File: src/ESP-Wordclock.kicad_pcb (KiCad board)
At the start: 2 copper layers, 100 x 100 mm, 1 part

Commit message: Add: BasePCB and added edge cut, holes, dimentions and LEDs with their caps
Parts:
- added BT401: CR2032, Battery:BatteryHolder_Keystone_3002_1x2032, F.Cu at (665.0, 195.0)
- added C1001: 0.1µF, Capacitor_SMD:C_0805_2012Metric_Pad1.18x1.45mm_HandSolder, F.Cu at (70.7, 105.8)
- added C1002: 0.1µF, Capacitor_SMD:C_0805_2012Metric_Pad1.18x1.45mm_HandSolder, F.Cu at (87.3, 105.8)
- added C1003: 0.1µF, Capacitor_SMD:C_0805_2012Metric_Pad1.18x1.45mm_HandSolder, F.Cu at (103.9, 105.8)
- added C1004: 0.1µF, Capacitor_SMD:C_0805_2012Metric_Pad1.18x1.45mm_HandSolder, F.Cu at (120.6, 105.8)
- added C1005: 0.1µF, Capacitor_SMD:C_0805_2012Metric_Pad1.18x1.45mm_HandSolder, F.Cu at (137.3, 105.8)
- added C1006: 0.1µF, Capacitor_SMD:C_0805_2012Metric_Pad1.18x1.45mm_HandSolder, F.Cu at (153.9, 105.8)
- added C1007: 0.1µF, Capacitor_SMD:C_0805_2012Metric_Pad1.18x1.45mm_HandSolder, F.Cu at (170.6, 105.8)
- added C1008: 0.1µF, Capacitor_SMD:C_0805_2012Metric_Pad1.18x1.45mm_HandSolder, F.Cu at (187.2, 105.8)
- added C1009: 0.1µF, Capacitor_SMD:C_0805_2012Metric_Pad1.18x1.45mm_HandSolder, F.Cu at (203.9, 105.8)
- added C1010: 0.1µF, Capacitor_SMD:C_0805_2012Metric_Pad1.18x1.45mm_HandSolder, F.Cu at (220.5, 105.8)
- added C1011: 0.1µF, Capacitor_SMD:C_0805_2012Metric_Pad1.18x1.45mm_HandSolder, F.Cu at (237.2, 105.8)
- added C1101: 0.1µF, Capacitor_SMD:C_0805_2012Metric_Pad1.18x1.45mm_HandSolder, F.Cu at (234.4, 115.8)
- added C1102: 0.1µF, Capacitor_SMD:C_0805_2012Metric_Pad1.18x1.45mm_HandSolder, F.Cu at (217.7, 115.8)
- added C1103: 0.1µF, Capacitor_SMD:C_0805_2012Metric_Pad1.18x1.45mm_HandSolder, F.Cu at (201.1, 115.8)
- added C1104: 0.1µF, Capacitor_SMD:C_0805_2012Metric_Pad1.18x1.45mm_HandSolder, F.Cu at (184.4, 115.8)
- added C1105: 0.1µF, Capacitor_SMD:C_0805_2012Metric_Pad1.18x1.45mm_HandSolder, F.Cu at (167.8, 115.8)
- added C1106: 0.1µF, Capacitor_SMD:C_0805_2012Metric_Pad1.18x1.45mm_HandSolder, F.Cu at (151.1, 115.8)
- added C1107: 0.1µF, Capacitor_SMD:C_0805_2012Metric_Pad1.18x1.45mm_HandSolder, F.Cu at (134.4, 115.8)
- added C1108: 0.1µF, Capacitor_SMD:C_0805_2012Metric_Pad1.18x1.45mm_HandSolder, F.Cu at (117.8, 115.8)
- added C1109: 0.1µF, Capacitor_SMD:C_0805_2012Metric_Pad1.18x1.45mm_HandSolder, F.Cu at (101.1, 115.8)
- added C1110: 0.1µF, Capacitor_SMD:C_0805_2012Metric_Pad1.18x1.45mm_HandSolder, F.Cu at (84.4, 115.8)
- added C1111: 0.1µF, Capacitor_SMD:C_0805_2012Metric_Pad1.18x1.45mm_HandSolder, F.Cu at (67.8, 115.8)
- added C1201: 0.1µF, Capacitor_SMD:C_0805_2012Metric_Pad1.18x1.45mm_HandSolder, F.Cu at (70.7, 142.5)
- added C1202: 0.1µF, Capacitor_SMD:C_0805_2012Metric_Pad1.18x1.45mm_HandSolder, F.Cu at (87.3, 142.5)
- added C1203: 0.1µF, Capacitor_SMD:C_0805_2012Metric_Pad1.18x1.45mm_HandSolder, F.Cu at (103.9, 142.5)
- added C1204: 0.1µF, Capacitor_SMD:C_0805_2012Metric_Pad1.18x1.45mm_HandSolder, F.Cu at (120.6, 142.5)
- added C1205: 0.1µF, Capacitor_SMD:C_0805_2012Metric_Pad1.18x1.45mm_HandSolder, F.Cu at (137.3, 142.5)
- added C1206: 0.1µF, Capacitor_SMD:C_0805_2012Metric_Pad1.18x1.45mm_HandSolder, F.Cu at (153.9, 142.5)
- added C1207: 0.1µF, Capacitor_SMD:C_0805_2012Metric_Pad1.18x1.45mm_HandSolder, F.Cu at (170.6, 142.5)
- added C1208: 0.1µF, Capacitor_SMD:C_0805_2012Metric_Pad1.18x1.45mm_HandSolder, F.Cu at (187.2, 142.5)
- added C1209: 0.1µF, Capacitor_SMD:C_0805_2012Metric_Pad1.18x1.45mm_HandSolder, F.Cu at (203.9, 142.5)
- added C1210: 0.1µF, Capacitor_SMD:C_0805_2012Metric_Pad1.18x1.45mm_HandSolder, F.Cu at (220.5, 142.5)
- added C1211: 0.1µF, Capacitor_SMD:C_0805_2012Metric_Pad1.18x1.45mm_HandSolder, F.Cu at (237.2, 142.5)
- added C1301: 0.1µF, Capacitor_SMD:C_0805_2012Metric_Pad1.18x1.45mm_HandSolder, F.Cu at (234.4, 152.5)
- added C1302: 0.1µF, Capacitor_SMD:C_0805_2012Metric_Pad1.18x1.45mm_HandSolder, F.Cu at (217.7, 152.5)
- added C1303: 0.1µF, Capacitor_SMD:C_0805_2012Metric_Pad1.18x1.45mm_HandSolder, F.Cu at (201.1, 152.5)
- added C1304: 0.1µF, Capacitor_SMD:C_0805_2012Metric_Pad1.18x1.45mm_HandSolder, F.Cu at (184.4, 152.5)
- added C1305: 0.1µF, Capacitor_SMD:C_0805_2012Metric_Pad1.18x1.45mm_HandSolder, F.Cu at (167.8, 152.5)
- added C1306: 0.1µF, Capacitor_SMD:C_0805_2012Metric_Pad1.18x1.45mm_HandSolder, F.Cu at (151.1, 152.5)
- added C1307: 0.1µF, Capacitor_SMD:C_0805_2012Metric_Pad1.18x1.45mm_HandSolder, F.Cu at (134.4, 152.5)
- added C1308: 0.1µF, Capacitor_SMD:C_0805_2012Metric_Pad1.18x1.45mm_HandSolder, F.Cu at (117.8, 152.5)
- added C1309: 0.1µF, Capacitor_SMD:C_0805_2012Metric_Pad1.18x1.45mm_HandSolder, F.Cu at (101.1, 152.5)
- added C1310: 0.1µF, Capacitor_SMD:C_0805_2012Metric_Pad1.18x1.45mm_HandSolder, F.Cu at (84.4, 152.5)
- added C1311: 0.1µF, Capacitor_SMD:C_0805_2012Metric_Pad1.18x1.45mm_HandSolder, F.Cu at (67.8, 152.5)
- added C1401: 0.1µF, Capacitor_SMD:C_0805_2012Metric_Pad1.18x1.45mm_HandSolder, F.Cu at (70.7, 179.1)
- added C1402: 0.1µF, Capacitor_SMD:C_0805_2012Metric_Pad1.18x1.45mm_HandSolder, F.Cu at (87.3, 179.1)
- added C1403: 0.1µF, Capacitor_SMD:C_0805_2012Metric_Pad1.18x1.45mm_HandSolder, F.Cu at (103.9, 179.1)
- added C1404: 0.1µF, Capacitor_SMD:C_0805_2012Metric_Pad1.18x1.45mm_HandSolder, F.Cu at (120.6, 179.1)
- added C1405: 0.1µF, Capacitor_SMD:C_0805_2012Metric_Pad1.18x1.45mm_HandSolder, F.Cu at (137.3, 179.1)
- added C1406: 0.1µF, Capacitor_SMD:C_0805_2012Metric_Pad1.18x1.45mm_HandSolder, F.Cu at (153.9, 179.1)
- added C1407: 0.1µF, Capacitor_SMD:C_0805_2012Metric_Pad1.18x1.45mm_HandSolder, F.Cu at (170.6, 179.1)
- added C1408: 0.1µF, Capacitor_SMD:C_0805_2012Metric_Pad1.18x1.45mm_HandSolder, F.Cu at (187.2, 179.1)
- added C1409: 0.1µF, Capacitor_SMD:C_0805_2012Metric_Pad1.18x1.45mm_HandSolder, F.Cu at (203.9, 179.1)
- added C1410: 0.1µF, Capacitor_SMD:C_0805_2012Metric_Pad1.18x1.45mm_HandSolder, F.Cu at (220.5, 179.1)
- added C1411: 0.1µF, Capacitor_SMD:C_0805_2012Metric_Pad1.18x1.45mm_HandSolder, F.Cu at (237.2, 179.1)
- added C1501: 0.1µF, Capacitor_SMD:C_0805_2012Metric_Pad1.18x1.45mm_HandSolder, F.Cu at (234.4, 189.2)
- added C1502: 0.1µF, Capacitor_SMD:C_0805_2012Metric_Pad1.18x1.45mm_HandSolder, F.Cu at (217.7, 189.2)
- added C1503: 0.1µF, Capacitor_SMD:C_0805_2012Metric_Pad1.18x1.45mm_HandSolder, F.Cu at (201.1, 189.2)
- added C1504: 0.1µF, Capacitor_SMD:C_0805_2012Metric_Pad1.18x1.45mm_HandSolder, F.Cu at (184.4, 189.2)
- added C1505: 0.1µF, Capacitor_SMD:C_0805_2012Metric_Pad1.18x1.45mm_HandSolder, F.Cu at (167.8, 189.2)
- added C1506: 0.1µF, Capacitor_SMD:C_0805_2012Metric_Pad1.18x1.45mm_HandSolder, F.Cu at (151.1, 189.2)
- added C1507: 0.1µF, Capacitor_SMD:C_0805_2012Metric_Pad1.18x1.45mm_HandSolder, F.Cu at (134.4, 189.2)
- added C1508: 0.1µF, Capacitor_SMD:C_0805_2012Metric_Pad1.18x1.45mm_HandSolder, F.Cu at (117.8, 189.2)
- added C1509: 0.1µF, Capacitor_SMD:C_0805_2012Metric_Pad1.18x1.45mm_HandSolder, F.Cu at (101.1, 189.2)
- added C1510: 0.1µF, Capacitor_SMD:C_0805_2012Metric_Pad1.18x1.45mm_HandSolder, F.Cu at (84.4, 189.2)
- added C1511: 0.1µF, Capacitor_SMD:C_0805_2012Metric_Pad1.18x1.45mm_HandSolder, F.Cu at (67.8, 189.2)
- added C1601: 0.1µF, Capacitor_SMD:C_0805_2012Metric_Pad1.18x1.45mm_HandSolder, F.Cu at (70.7, 215.8)
- added C1602: 0.1µF, Capacitor_SMD:C_0805_2012Metric_Pad1.18x1.45mm_HandSolder, F.Cu at (87.3, 215.8)
- added C1603: 0.1µF, Capacitor_SMD:C_0805_2012Metric_Pad1.18x1.45mm_HandSolder, F.Cu at (103.9, 215.8)
- added C1604: 0.1µF, Capacitor_SMD:C_0805_2012Metric_Pad1.18x1.45mm_HandSolder, F.Cu at (120.6, 215.8)
- added C1605: 0.1µF, Capacitor_SMD:C_0805_2012Metric_Pad1.18x1.45mm_HandSolder, F.Cu at (137.3, 215.8)
- added C1606: 0.1µF, Capacitor_SMD:C_0805_2012Metric_Pad1.18x1.45mm_HandSolder, F.Cu at (153.9, 215.8)
- added C1607: 0.1µF, Capacitor_SMD:C_0805_2012Metric_Pad1.18x1.45mm_HandSolder, F.Cu at (170.6, 215.8)
- added C1608: 0.1µF, Capacitor_SMD:C_0805_2012Metric_Pad1.18x1.45mm_HandSolder, F.Cu at (187.2, 215.8)
- added C1609: 0.1µF, Capacitor_SMD:C_0805_2012Metric_Pad1.18x1.45mm_HandSolder, F.Cu at (203.9, 215.8)
- added C1610: 0.1µF, Capacitor_SMD:C_0805_2012Metric_Pad1.18x1.45mm_HandSolder, F.Cu at (220.5, 215.8)
- added C1611: 0.1µF, Capacitor_SMD:C_0805_2012Metric_Pad1.18x1.45mm_HandSolder, F.Cu at (237.2, 215.8)
- added C1701: 0.1µF, Capacitor_SMD:C_0805_2012Metric_Pad1.18x1.45mm_HandSolder, F.Cu at (234.4, 225.9)
- added C1702: 0.1µF, Capacitor_SMD:C_0805_2012Metric_Pad1.18x1.45mm_HandSolder, F.Cu at (217.7, 225.9)
- added C1703: 0.1µF, Capacitor_SMD:C_0805_2012Metric_Pad1.18x1.45mm_HandSolder, F.Cu at (201.1, 225.9)
- added C1704: 0.1µF, Capacitor_SMD:C_0805_2012Metric_Pad1.18x1.45mm_HandSolder, F.Cu at (184.4, 225.9)
- added C1705: 0.1µF, Capacitor_SMD:C_0805_2012Metric_Pad1.18x1.45mm_HandSolder, F.Cu at (167.8, 225.9)
- added C1706: 0.1µF, Capacitor_SMD:C_0805_2012Metric_Pad1.18x1.45mm_HandSolder, F.Cu at (151.1, 225.9)
- added C1707: 0.1µF, Capacitor_SMD:C_0805_2012Metric_Pad1.18x1.45mm_HandSolder, F.Cu at (134.4, 225.9)
- added C1708: 0.1µF, Capacitor_SMD:C_0805_2012Metric_Pad1.18x1.45mm_HandSolder, F.Cu at (117.8, 225.9)
- added C1709: 0.1µF, Capacitor_SMD:C_0805_2012Metric_Pad1.18x1.45mm_HandSolder, F.Cu at (101.1, 225.9)
- added C1710: 0.1µF, Capacitor_SMD:C_0805_2012Metric_Pad1.18x1.45mm_HandSolder, F.Cu at (84.4, 225.9)
- added C1711: 0.1µF, Capacitor_SMD:C_0805_2012Metric_Pad1.18x1.45mm_HandSolder, F.Cu at (67.8, 225.9)
- added C201: 0.1µF, Capacitor_SMD:C_0805_2012Metric_Pad1.18x1.45mm_HandSolder, F.Cu at (713.3, 142.5)
- added C202: 10µF, Capacitor_SMD:C_0805_2012Metric_Pad1.18x1.45mm_HandSolder, F.Cu at (713.3, 145.5)
- added C203: 1µF, Capacitor_SMD:C_0805_2012Metric_Pad1.18x1.45mm_HandSolder, F.Cu at (713.3, 148.5)
- added C204: 10µF, Capacitor_SMD:C_0805_2012Metric_Pad1.18x1.45mm_HandSolder, F.Cu at (713.3, 151.5)
- added C205: 10µF, Capacitor_SMD:C_0805_2012Metric_Pad1.18x1.45mm_HandSolder, F.Cu at (713.3, 154.6)
- added C206: 0.1µF, Capacitor_SMD:C_0805_2012Metric_Pad1.18x1.45mm_HandSolder, F.Cu at (713.3, 157.6)
- added C207: 0.1µF, Capacitor_SMD:C_0805_2012Metric_Pad1.18x1.45mm_HandSolder, F.Cu at (713.3, 160.6)
- added C208: 0.1µF, Capacitor_SMD:C_0805_2012Metric_Pad1.18x1.45mm_HandSolder, F.Cu at (713.3, 163.6)
- added C301: 10µF, Capacitor_SMD:C_0805_2012Metric_Pad1.18x1.45mm_HandSolder, F.Cu at (516.6, 36.1)
- added C302: 0.1µF, Capacitor_SMD:C_0805_2012Metric_Pad1.18x1.45mm_HandSolder, F.Cu at (516.6, 39.1)
- added C303: 0.1µF, Capacitor_SMD:C_0805_2012Metric_Pad1.18x1.45mm_HandSolder, F.Cu at (516.6, 42.1)
- added C304: 0.1µF, Capacitor_SMD:C_0805_2012Metric_Pad1.18x1.45mm_HandSolder, F.Cu at (516.6, 45.2)
- added C305: 1µF, Capacitor_SMD:C_0805_2012Metric_Pad1.18x1.45mm_HandSolder, F.Cu at (516.6, 48.2)
- added C306: 10µF, Capacitor_SMD:C_0805_2012Metric_Pad1.18x1.45mm_HandSolder, F.Cu at (516.6, 51.2)
- added C307: 0.1µF, Capacitor_SMD:C_0805_2012Metric_Pad1.18x1.45mm_HandSolder, F.Cu at (516.6, 54.2)
- added C308: 0.1µF, Capacitor_SMD:C_0805_2012Metric_Pad1.18x1.45mm_HandSolder, F.Cu at (516.6, 57.2)
- added C309: 10µF, Capacitor_SMD:C_0805_2012Metric_Pad1.18x1.45mm_HandSolder, F.Cu at (516.6, 60.2)
- added C401: 10µF, Capacitor_SMD:C_0805_2012Metric_Pad1.18x1.45mm_HandSolder, F.Cu at (668.7, 208.1)
- added C402: 0.1µF, Capacitor_SMD:C_0805_2012Metric_Pad1.18x1.45mm_HandSolder, F.Cu at (668.7, 211.1)
- added C403: 1µF, Capacitor_SMD:C_0805_2012Metric_Pad1.18x1.45mm_HandSolder, F.Cu at (668.7, 214.1)
- added C404: 0.1µF, Capacitor_SMD:C_0805_2012Metric_Pad1.18x1.45mm_HandSolder, F.Cu at (668.7, 217.2)
- added C501: 10µF, Capacitor_SMD:C_0805_2012Metric_Pad1.18x1.45mm_HandSolder, F.Cu at (706.2, 98.6)
- added C502: 0.1µF, Capacitor_SMD:C_0805_2012Metric_Pad1.18x1.45mm_HandSolder, F.Cu at (706.2, 101.6)
- added C503: 10µF, Capacitor_SMD:C_0805_2012Metric_Pad1.18x1.45mm_HandSolder, F.Cu at (706.2, 104.7)
- added C504: 0.1µF, Capacitor_SMD:C_0805_2012Metric_Pad1.18x1.45mm_HandSolder, F.Cu at (706.2, 107.7)
- added C505: 1µF, Capacitor_SMD:C_0805_2012Metric_Pad1.18x1.45mm_HandSolder, F.Cu at (706.2, 110.7)
- added C701: 0.1µF, Capacitor_SMD:C_0805_2012Metric_Pad1.18x1.45mm_HandSolder, F.Cu at (103.9, 249.1)
- added C702: 0.1µF, Capacitor_SMD:C_0805_2012Metric_Pad1.18x1.45mm_HandSolder, F.Cu at (137.3, 249.1)
- added C703: 0.1µF, Capacitor_SMD:C_0805_2012Metric_Pad1.18x1.45mm_HandSolder, F.Cu at (170.6, 249.1)
- added C704: 0.1µF, Capacitor_SMD:C_0805_2012Metric_Pad1.18x1.45mm_HandSolder, F.Cu at (203.9, 249.1)
- added C801: 0.1µF, Capacitor_SMD:C_0805_2012Metric_Pad1.18x1.45mm_HandSolder, F.Cu at (70.7, 69.1)
- added C802: 0.1µF, Capacitor_SMD:C_0805_2012Metric_Pad1.18x1.45mm_HandSolder, F.Cu at (87.3, 69.1)
- added C803: 0.1µF, Capacitor_SMD:C_0805_2012Metric_Pad1.18x1.45mm_HandSolder, F.Cu at (103.9, 69.1)
- added C804: 0.1µF, Capacitor_SMD:C_0805_2012Metric_Pad1.18x1.45mm_HandSolder, F.Cu at (120.6, 69.1)
- added C805: 0.1µF, Capacitor_SMD:C_0805_2012Metric_Pad1.18x1.45mm_HandSolder, F.Cu at (137.3, 69.1)
- added C806: 0.1µF, Capacitor_SMD:C_0805_2012Metric_Pad1.18x1.45mm_HandSolder, F.Cu at (153.9, 69.1)
- added C807: 0.1µF, Capacitor_SMD:C_0805_2012Metric_Pad1.18x1.45mm_HandSolder, F.Cu at (170.6, 69.1)
- added C808: 0.1µF, Capacitor_SMD:C_0805_2012Metric_Pad1.18x1.45mm_HandSolder, F.Cu at (187.2, 69.1)
- added C809: 0.1µF, Capacitor_SMD:C_0805_2012Metric_Pad1.18x1.45mm_HandSolder, F.Cu at (203.9, 69.1)
- added C810: 0.1µF, Capacitor_SMD:C_0805_2012Metric_Pad1.18x1.45mm_HandSolder, F.Cu at (220.5, 69.1)
- added C811: 0.1µF, Capacitor_SMD:C_0805_2012Metric_Pad1.18x1.45mm_HandSolder, F.Cu at (237.2, 69.1)
- added C901: 0.1µF, Capacitor_SMD:C_0805_2012Metric_Pad1.18x1.45mm_HandSolder, F.Cu at (234.4, 79.2)
- added C902: 0.1µF, Capacitor_SMD:C_0805_2012Metric_Pad1.18x1.45mm_HandSolder, F.Cu at (217.7, 79.2)
- added C903: 0.1µF, Capacitor_SMD:C_0805_2012Metric_Pad1.18x1.45mm_HandSolder, F.Cu at (201.1, 79.2)
- added C904: 0.1µF, Capacitor_SMD:C_0805_2012Metric_Pad1.18x1.45mm_HandSolder, F.Cu at (184.4, 79.2)
- added C905: 0.1µF, Capacitor_SMD:C_0805_2012Metric_Pad1.18x1.45mm_HandSolder, F.Cu at (167.8, 79.2)
- added C906: 0.1µF, Capacitor_SMD:C_0805_2012Metric_Pad1.18x1.45mm_HandSolder, F.Cu at (151.1, 79.2)
- added C907: 0.1µF, Capacitor_SMD:C_0805_2012Metric_Pad1.18x1.45mm_HandSolder, F.Cu at (134.4, 79.2)
- added C908: 0.1µF, Capacitor_SMD:C_0805_2012Metric_Pad1.18x1.45mm_HandSolder, F.Cu at (117.8, 79.2)
- added C909: 0.1µF, Capacitor_SMD:C_0805_2012Metric_Pad1.18x1.45mm_HandSolder, F.Cu at (101.1, 79.2)
- added C910: 0.1µF, Capacitor_SMD:C_0805_2012Metric_Pad1.18x1.45mm_HandSolder, F.Cu at (84.4, 79.2)
- added C911: 0.1µF, Capacitor_SMD:C_0805_2012Metric_Pad1.18x1.45mm_HandSolder, F.Cu at (67.8, 79.2)
- added D1001: WS2812B, LED_SMD:LED_WS2812B_PLCC4_5.0x5.0mm_P3.2mm, F.Cu at (69.2, 101.7)
- added D1002: WS2812B, LED_SMD:LED_WS2812B_PLCC4_5.0x5.0mm_P3.2mm, F.Cu at (85.9, 101.7)
- added D1003: WS2812B, LED_SMD:LED_WS2812B_PLCC4_5.0x5.0mm_P3.2mm, F.Cu at (102.5, 101.7)
- added D1004: WS2812B, LED_SMD:LED_WS2812B_PLCC4_5.0x5.0mm_P3.2mm, F.Cu at (119.2, 101.7)
- added D1005: WS2812B, LED_SMD:LED_WS2812B_PLCC4_5.0x5.0mm_P3.2mm, F.Cu at (135.8, 101.7)
- added D1006: WS2812B, LED_SMD:LED_WS2812B_PLCC4_5.0x5.0mm_P3.2mm, F.Cu at (152.5, 101.7)
- added D1007: WS2812B, LED_SMD:LED_WS2812B_PLCC4_5.0x5.0mm_P3.2mm, F.Cu at (169.2, 101.7)
- added D1008: WS2812B, LED_SMD:LED_WS2812B_PLCC4_5.0x5.0mm_P3.2mm, F.Cu at (185.8, 101.7)
- added D1009: WS2812B, LED_SMD:LED_WS2812B_PLCC4_5.0x5.0mm_P3.2mm, F.Cu at (202.5, 101.7)
- added D1010: WS2812B, LED_SMD:LED_WS2812B_PLCC4_5.0x5.0mm_P3.2mm, F.Cu at (219.1, 101.7)
- added D1011: WS2812B, LED_SMD:LED_WS2812B_PLCC4_5.0x5.0mm_P3.2mm, F.Cu at (235.8, 101.7)
- added D1101: WS2812B, LED_SMD:LED_WS2812B_PLCC4_5.0x5.0mm_P3.2mm, F.Cu at (235.8, 120.0)
- added D1102: WS2812B, LED_SMD:LED_WS2812B_PLCC4_5.0x5.0mm_P3.2mm, F.Cu at (219.1, 120.0)
- added D1103: WS2812B, LED_SMD:LED_WS2812B_PLCC4_5.0x5.0mm_P3.2mm, F.Cu at (202.5, 120.0)
- added D1104: WS2812B, LED_SMD:LED_WS2812B_PLCC4_5.0x5.0mm_P3.2mm, F.Cu at (185.8, 120.0)
- added D1105: WS2812B, LED_SMD:LED_WS2812B_PLCC4_5.0x5.0mm_P3.2mm, F.Cu at (169.2, 120.0)
- added D1106: WS2812B, LED_SMD:LED_WS2812B_PLCC4_5.0x5.0mm_P3.2mm, F.Cu at (152.5, 120.0)
- added D1107: WS2812B, LED_SMD:LED_WS2812B_PLCC4_5.0x5.0mm_P3.2mm, F.Cu at (135.8, 120.0)
- added D1108: WS2812B, LED_SMD:LED_WS2812B_PLCC4_5.0x5.0mm_P3.2mm, F.Cu at (119.2, 120.0)
- added D1109: WS2812B, LED_SMD:LED_WS2812B_PLCC4_5.0x5.0mm_P3.2mm, F.Cu at (102.5, 120.0)
- added D1110: WS2812B, LED_SMD:LED_WS2812B_PLCC4_5.0x5.0mm_P3.2mm, F.Cu at (85.9, 120.0)
- added D1111: WS2812B, LED_SMD:LED_WS2812B_PLCC4_5.0x5.0mm_P3.2mm, F.Cu at (69.2, 120.0)
- added D1201: WS2812B, LED_SMD:LED_WS2812B_PLCC4_5.0x5.0mm_P3.2mm, F.Cu at (69.2, 138.3)
- added D1202: WS2812B, LED_SMD:LED_WS2812B_PLCC4_5.0x5.0mm_P3.2mm, F.Cu at (85.9, 138.3)
- added D1203: WS2812B, LED_SMD:LED_WS2812B_PLCC4_5.0x5.0mm_P3.2mm, F.Cu at (102.5, 138.3)
- added D1204: WS2812B, LED_SMD:LED_WS2812B_PLCC4_5.0x5.0mm_P3.2mm, F.Cu at (119.2, 138.3)
- added D1205: WS2812B, LED_SMD:LED_WS2812B_PLCC4_5.0x5.0mm_P3.2mm, F.Cu at (135.8, 138.3)
- added D1206: WS2812B, LED_SMD:LED_WS2812B_PLCC4_5.0x5.0mm_P3.2mm, F.Cu at (152.5, 138.3)
- added D1207: WS2812B, LED_SMD:LED_WS2812B_PLCC4_5.0x5.0mm_P3.2mm, F.Cu at (169.2, 138.3)
- added D1208: WS2812B, LED_SMD:LED_WS2812B_PLCC4_5.0x5.0mm_P3.2mm, F.Cu at (185.8, 138.3)
- added D1209: WS2812B, LED_SMD:LED_WS2812B_PLCC4_5.0x5.0mm_P3.2mm, F.Cu at (202.5, 138.3)
- added D1210: WS2812B, LED_SMD:LED_WS2812B_PLCC4_5.0x5.0mm_P3.2mm, F.Cu at (219.1, 138.3)
- added D1211: WS2812B, LED_SMD:LED_WS2812B_PLCC4_5.0x5.0mm_P3.2mm, F.Cu at (235.8, 138.3)
- added D1301: WS2812B, LED_SMD:LED_WS2812B_PLCC4_5.0x5.0mm_P3.2mm, F.Cu at (235.8, 156.7)
- added D1302: WS2812B, LED_SMD:LED_WS2812B_PLCC4_5.0x5.0mm_P3.2mm, F.Cu at (219.1, 156.7)
- added D1303: WS2812B, LED_SMD:LED_WS2812B_PLCC4_5.0x5.0mm_P3.2mm, F.Cu at (202.5, 156.7)
- added D1304: WS2812B, LED_SMD:LED_WS2812B_PLCC4_5.0x5.0mm_P3.2mm, F.Cu at (185.8, 156.7)
- added D1305: WS2812B, LED_SMD:LED_WS2812B_PLCC4_5.0x5.0mm_P3.2mm, F.Cu at (169.2, 156.7)
- added D1306: WS2812B, LED_SMD:LED_WS2812B_PLCC4_5.0x5.0mm_P3.2mm, F.Cu at (152.5, 156.7)
- added D1307: WS2812B, LED_SMD:LED_WS2812B_PLCC4_5.0x5.0mm_P3.2mm, F.Cu at (135.8, 156.7)
- added D1308: WS2812B, LED_SMD:LED_WS2812B_PLCC4_5.0x5.0mm_P3.2mm, F.Cu at (119.2, 156.7)
- added D1309: WS2812B, LED_SMD:LED_WS2812B_PLCC4_5.0x5.0mm_P3.2mm, F.Cu at (102.5, 156.7)
- added D1310: WS2812B, LED_SMD:LED_WS2812B_PLCC4_5.0x5.0mm_P3.2mm, F.Cu at (85.9, 156.7)
- added D1311: WS2812B, LED_SMD:LED_WS2812B_PLCC4_5.0x5.0mm_P3.2mm, F.Cu at (69.2, 156.7)
- added D1401: WS2812B, LED_SMD:LED_WS2812B_PLCC4_5.0x5.0mm_P3.2mm, F.Cu at (69.2, 175.0)
- added D1402: WS2812B, LED_SMD:LED_WS2812B_PLCC4_5.0x5.0mm_P3.2mm, F.Cu at (85.9, 175.0)
- added D1403: WS2812B, LED_SMD:LED_WS2812B_PLCC4_5.0x5.0mm_P3.2mm, F.Cu at (102.5, 175.0)
- added D1404: WS2812B, LED_SMD:LED_WS2812B_PLCC4_5.0x5.0mm_P3.2mm, F.Cu at (119.2, 175.0)
- added D1405: WS2812B, LED_SMD:LED_WS2812B_PLCC4_5.0x5.0mm_P3.2mm, F.Cu at (135.8, 175.0)
- added D1406: WS2812B, LED_SMD:LED_WS2812B_PLCC4_5.0x5.0mm_P3.2mm, F.Cu at (152.5, 175.0)
- added D1407: WS2812B, LED_SMD:LED_WS2812B_PLCC4_5.0x5.0mm_P3.2mm, F.Cu at (169.2, 175.0)
- added D1408: WS2812B, LED_SMD:LED_WS2812B_PLCC4_5.0x5.0mm_P3.2mm, F.Cu at (185.8, 175.0)
- added D1409: WS2812B, LED_SMD:LED_WS2812B_PLCC4_5.0x5.0mm_P3.2mm, F.Cu at (202.5, 175.0)
- added D1410: WS2812B, LED_SMD:LED_WS2812B_PLCC4_5.0x5.0mm_P3.2mm, F.Cu at (219.1, 175.0)
- added D1411: WS2812B, LED_SMD:LED_WS2812B_PLCC4_5.0x5.0mm_P3.2mm, F.Cu at (235.8, 175.0)
- added D1501: WS2812B, LED_SMD:LED_WS2812B_PLCC4_5.0x5.0mm_P3.2mm, F.Cu at (235.8, 193.3)
- added D1502: WS2812B, LED_SMD:LED_WS2812B_PLCC4_5.0x5.0mm_P3.2mm, F.Cu at (219.1, 193.3)
- added D1503: WS2812B, LED_SMD:LED_WS2812B_PLCC4_5.0x5.0mm_P3.2mm, F.Cu at (202.5, 193.3)
- added D1504: WS2812B, LED_SMD:LED_WS2812B_PLCC4_5.0x5.0mm_P3.2mm, F.Cu at (185.8, 193.3)
- added D1505: WS2812B, LED_SMD:LED_WS2812B_PLCC4_5.0x5.0mm_P3.2mm, F.Cu at (169.2, 193.3)
- added D1506: WS2812B, LED_SMD:LED_WS2812B_PLCC4_5.0x5.0mm_P3.2mm, F.Cu at (152.5, 193.3)
- added D1507: WS2812B, LED_SMD:LED_WS2812B_PLCC4_5.0x5.0mm_P3.2mm, F.Cu at (135.8, 193.3)
- added D1508: WS2812B, LED_SMD:LED_WS2812B_PLCC4_5.0x5.0mm_P3.2mm, F.Cu at (119.2, 193.3)
- added D1509: WS2812B, LED_SMD:LED_WS2812B_PLCC4_5.0x5.0mm_P3.2mm, F.Cu at (102.5, 193.3)
- added D1510: WS2812B, LED_SMD:LED_WS2812B_PLCC4_5.0x5.0mm_P3.2mm, F.Cu at (85.9, 193.3)
- added D1511: WS2812B, LED_SMD:LED_WS2812B_PLCC4_5.0x5.0mm_P3.2mm, F.Cu at (69.2, 193.3)
- added D1601: WS2812B, LED_SMD:LED_WS2812B_PLCC4_5.0x5.0mm_P3.2mm, F.Cu at (69.2, 211.7)
- added D1602: WS2812B, LED_SMD:LED_WS2812B_PLCC4_5.0x5.0mm_P3.2mm, F.Cu at (85.9, 211.7)
- added D1603: WS2812B, LED_SMD:LED_WS2812B_PLCC4_5.0x5.0mm_P3.2mm, F.Cu at (102.5, 211.7)
- added D1604: WS2812B, LED_SMD:LED_WS2812B_PLCC4_5.0x5.0mm_P3.2mm, F.Cu at (119.2, 211.7)
- added D1605: WS2812B, LED_SMD:LED_WS2812B_PLCC4_5.0x5.0mm_P3.2mm, F.Cu at (135.8, 211.7)
- added D1606: WS2812B, LED_SMD:LED_WS2812B_PLCC4_5.0x5.0mm_P3.2mm, F.Cu at (152.5, 211.7)
- added D1607: WS2812B, LED_SMD:LED_WS2812B_PLCC4_5.0x5.0mm_P3.2mm, F.Cu at (169.2, 211.7)
- added D1608: WS2812B, LED_SMD:LED_WS2812B_PLCC4_5.0x5.0mm_P3.2mm, F.Cu at (185.8, 211.7)
- added D1609: WS2812B, LED_SMD:LED_WS2812B_PLCC4_5.0x5.0mm_P3.2mm, F.Cu at (202.5, 211.7)
- added D1610: WS2812B, LED_SMD:LED_WS2812B_PLCC4_5.0x5.0mm_P3.2mm, F.Cu at (219.1, 211.7)
- added D1611: WS2812B, LED_SMD:LED_WS2812B_PLCC4_5.0x5.0mm_P3.2mm, F.Cu at (235.8, 211.7)
- added D1701: WS2812B, LED_SMD:LED_WS2812B_PLCC4_5.0x5.0mm_P3.2mm, F.Cu at (235.8, 230.0)
- added D1702: WS2812B, LED_SMD:LED_WS2812B_PLCC4_5.0x5.0mm_P3.2mm, F.Cu at (219.1, 230.0)
- added D1703: WS2812B, LED_SMD:LED_WS2812B_PLCC4_5.0x5.0mm_P3.2mm, F.Cu at (202.5, 230.0)
- added D1704: WS2812B, LED_SMD:LED_WS2812B_PLCC4_5.0x5.0mm_P3.2mm, F.Cu at (185.8, 230.0)
- added D1705: WS2812B, LED_SMD:LED_WS2812B_PLCC4_5.0x5.0mm_P3.2mm, F.Cu at (169.2, 230.0)
- added D1706: WS2812B, LED_SMD:LED_WS2812B_PLCC4_5.0x5.0mm_P3.2mm, F.Cu at (152.5, 230.0)
- added D1707: WS2812B, LED_SMD:LED_WS2812B_PLCC4_5.0x5.0mm_P3.2mm, F.Cu at (135.8, 230.0)
- added D1708: WS2812B, LED_SMD:LED_WS2812B_PLCC4_5.0x5.0mm_P3.2mm, F.Cu at (119.2, 230.0)
- added D1709: WS2812B, LED_SMD:LED_WS2812B_PLCC4_5.0x5.0mm_P3.2mm, F.Cu at (102.5, 230.0)
- added D1710: WS2812B, LED_SMD:LED_WS2812B_PLCC4_5.0x5.0mm_P3.2mm, F.Cu at (85.9, 230.0)
- added D1711: WS2812B, LED_SMD:LED_WS2812B_PLCC4_5.0x5.0mm_P3.2mm, F.Cu at (69.2, 230.0)
- added D201: SP0503BAHT, Package_TO_SOT_SMD:SOT-143_Handsoldering, F.Cu at (733.1, 143.4)
- added D202: green, LED_SMD:LED_0805_2012Metric_Pad1.15x1.40mm_HandSolder, F.Cu at (736.2, 157.3)
- added D203: green, LED_SMD:LED_0805_2012Metric_Pad1.15x1.40mm_HandSolder, F.Cu at (736.2, 160.3)
- added D301: red, LED_SMD:LED_0805_2012Metric_Pad1.15x1.40mm_HandSolder, F.Cu at (542.7, 62.7)
- added D302: orange, LED_SMD:LED_0805_2012Metric_Pad1.15x1.40mm_HandSolder, F.Cu at (542.7, 65.7)
- added D701: WS2812B, LED_SMD:LED_WS2812B_PLCC4_5.0x5.0mm_P3.2mm, F.Cu at (102.5, 245.0)
- added D702: WS2812B, LED_SMD:LED_WS2812B_PLCC4_5.0x5.0mm_P3.2mm, F.Cu at (135.8, 245.0)
- added D703: WS2812B, LED_SMD:LED_WS2812B_PLCC4_5.0x5.0mm_P3.2mm, F.Cu at (169.2, 245.0)
- added D704: WS2812B, LED_SMD:LED_WS2812B_PLCC4_5.0x5.0mm_P3.2mm, F.Cu at (202.5, 245.0)
- added D801: WS2812B, LED_SMD:LED_WS2812B_PLCC4_5.0x5.0mm_P3.2mm, F.Cu at (69.2, 65.0)
- added D802: WS2812B, LED_SMD:LED_WS2812B_PLCC4_5.0x5.0mm_P3.2mm, F.Cu at (85.9, 65.0)
- added D803: WS2812B, LED_SMD:LED_WS2812B_PLCC4_5.0x5.0mm_P3.2mm, F.Cu at (102.5, 65.0)
- added D804: WS2812B, LED_SMD:LED_WS2812B_PLCC4_5.0x5.0mm_P3.2mm, F.Cu at (119.2, 65.0)
- added D805: WS2812B, LED_SMD:LED_WS2812B_PLCC4_5.0x5.0mm_P3.2mm, F.Cu at (135.8, 65.0)
- added D806: WS2812B, LED_SMD:LED_WS2812B_PLCC4_5.0x5.0mm_P3.2mm, F.Cu at (152.5, 65.0)
- added D807: WS2812B, LED_SMD:LED_WS2812B_PLCC4_5.0x5.0mm_P3.2mm, F.Cu at (169.2, 65.0)
- added D808: WS2812B, LED_SMD:LED_WS2812B_PLCC4_5.0x5.0mm_P3.2mm, F.Cu at (185.8, 65.0)
- added D809: WS2812B, LED_SMD:LED_WS2812B_PLCC4_5.0x5.0mm_P3.2mm, F.Cu at (202.5, 65.0)
- added D810: WS2812B, LED_SMD:LED_WS2812B_PLCC4_5.0x5.0mm_P3.2mm, F.Cu at (219.1, 65.0)
- added D811: WS2812B, LED_SMD:LED_WS2812B_PLCC4_5.0x5.0mm_P3.2mm, F.Cu at (235.8, 65.0)
- added D901: WS2812B, LED_SMD:LED_WS2812B_PLCC4_5.0x5.0mm_P3.2mm, F.Cu at (235.8, 83.3)
- added D902: WS2812B, LED_SMD:LED_WS2812B_PLCC4_5.0x5.0mm_P3.2mm, F.Cu at (219.1, 83.3)
- added D903: WS2812B, LED_SMD:LED_WS2812B_PLCC4_5.0x5.0mm_P3.2mm, F.Cu at (202.5, 83.3)
- added D904: WS2812B, LED_SMD:LED_WS2812B_PLCC4_5.0x5.0mm_P3.2mm, F.Cu at (185.8, 83.3)
- added D905: WS2812B, LED_SMD:LED_WS2812B_PLCC4_5.0x5.0mm_P3.2mm, F.Cu at (169.2, 83.3)
- added D906: WS2812B, LED_SMD:LED_WS2812B_PLCC4_5.0x5.0mm_P3.2mm, F.Cu at (152.5, 83.3)
- added D907: WS2812B, LED_SMD:LED_WS2812B_PLCC4_5.0x5.0mm_P3.2mm, F.Cu at (135.8, 83.3)
- added D908: WS2812B, LED_SMD:LED_WS2812B_PLCC4_5.0x5.0mm_P3.2mm, F.Cu at (119.2, 83.3)
- added D909: WS2812B, LED_SMD:LED_WS2812B_PLCC4_5.0x5.0mm_P3.2mm, F.Cu at (102.5, 83.3)
- added D910: WS2812B, LED_SMD:LED_WS2812B_PLCC4_5.0x5.0mm_P3.2mm, F.Cu at (85.9, 83.3)
- added D911: WS2812B, LED_SMD:LED_WS2812B_PLCC4_5.0x5.0mm_P3.2mm, F.Cu at (69.2, 83.3)
- added J101: Conn_01x08_Pin, Connector_PinHeader_2.54mm:PinHeader_1x08_P2.54mm_Vertical, F.Cu at (662.2, 57.6)
- added J201: USB_C_Receptacle_USB2.0_16P, Connector_USB:USB_C_Receptacle_GCT_USB4105-xx-A_16P_TopMnt_Horizontal, F.Cu at (721.5, 161.0)
- added JP501: SolderJumper_2_Open, Jumper:SolderJumper-2_P1.3mm_Open_RoundedPad1.0x1.5mm, F.Cu at (715.5, 108.0)
- added Q201: NPN BJT, Package_TO_SOT_SMD:SOT-23_Handsoldering, F.Cu at (730.6, 158.3)
- added Q202: NPN BJT, Package_TO_SOT_SMD:SOT-23_Handsoldering, F.Cu at (730.6, 163.0)
- added Q601: BSS138, Package_TO_SOT_SMD:SOT-23_Handsoldering, F.Cu at (678.0, 86.2)
- added R201: 0R, Resistor_SMD:R_0805_2012Metric_Pad1.20x1.40mm_HandSolder, F.Cu at (718.1, 142.5)
- added R202: 5.1k, Resistor_SMD:R_0805_2012Metric_Pad1.20x1.40mm_HandSolder, F.Cu at (718.1, 145.4)
- added R203: 5.1k, Resistor_SMD:R_0805_2012Metric_Pad1.20x1.40mm_HandSolder, F.Cu at (718.1, 148.4)
- added R204: 0R, Resistor_SMD:R_0805_2012Metric_Pad1.20x1.40mm_HandSolder, F.Cu at (718.1, 151.3)
- added R205: 0R, Resistor_SMD:R_0805_2012Metric_Pad1.20x1.40mm_HandSolder, F.Cu at (718.1, 154.3)
- added R206: 22.1k, Resistor_SMD:R_0805_2012Metric_Pad1.20x1.40mm_HandSolder, F.Cu at (722.8, 142.5)
- added R207: 47.5k, Resistor_SMD:R_0805_2012Metric_Pad1.20x1.40mm_HandSolder, F.Cu at (722.8, 145.4)
- added R208: 0R, Resistor_SMD:R_0805_2012Metric_Pad1.20x1.40mm_HandSolder, F.Cu at (722.8, 148.4)
- added R209: 0R, Resistor_SMD:R_0805_2012Metric_Pad1.20x1.40mm_HandSolder, F.Cu at (722.8, 151.3)
- added R210: 1k, Resistor_SMD:R_0805_2012Metric_Pad1.20x1.40mm_HandSolder, F.Cu at (722.8, 154.3)
- added R211: 10k, Resistor_SMD:R_0805_2012Metric_Pad1.20x1.40mm_HandSolder, F.Cu at (727.6, 142.5)
- added R212: 10k, Resistor_SMD:R_0805_2012Metric_Pad1.20x1.40mm_HandSolder, F.Cu at (727.6, 145.4)
- added R213: 1k, Resistor_SMD:R_0805_2012Metric_Pad1.20x1.40mm_HandSolder, F.Cu at (727.6, 148.4)
- added R214: 1k, Resistor_SMD:R_0805_2012Metric_Pad1.20x1.40mm_HandSolder, F.Cu at (727.6, 151.3)
- added R301: 10k, Resistor_SMD:R_0805_2012Metric_Pad1.20x1.40mm_HandSolder, F.Cu at (521.4, 62.6)
- added R302: 10k, Resistor_SMD:R_0805_2012Metric_Pad1.20x1.40mm_HandSolder, F.Cu at (521.4, 65.6)
- added R303: 5.1k, Resistor_SMD:R_0805_2012Metric_Pad1.20x1.40mm_HandSolder, F.Cu at (521.4, 68.5)
- added R304: 1k, Resistor_SMD:R_0805_2012Metric_Pad1.20x1.40mm_HandSolder, F.Cu at (521.4, 71.5)
- added R401: 0R, Resistor_SMD:R_0805_2012Metric_Pad1.20x1.40mm_HandSolder, F.Cu at (651.0, 208.1)
- added R402: 10k, Resistor_SMD:R_0805_2012Metric_Pad1.20x1.40mm_HandSolder, F.Cu at (651.0, 211.0)
- added R403: 10k, Resistor_SMD:R_0805_2012Metric_Pad1.20x1.40mm_HandSolder, F.Cu at (651.0, 214.0)
- added R404: 0R, Resistor_SMD:R_0805_2012Metric_Pad1.20x1.40mm_HandSolder, F.Cu at (651.0, 216.9)
- added R405: 0R, Resistor_SMD:R_0805_2012Metric_Pad1.20x1.40mm_HandSolder, F.Cu at (651.0, 219.9)
- added R501: 10k, Resistor_SMD:R_0805_2012Metric_Pad1.20x1.40mm_HandSolder, F.Cu at (711.0, 98.6)
- added R502: LDR07, OptoDevice:R_LDR_5.1x4.3mm_P3.4mm_Vertical, F.Cu at (715.0, 100.0)
- added R503: 0R, Resistor_SMD:R_0805_2012Metric_Pad1.20x1.40mm_HandSolder, F.Cu at (711.0, 101.5)
- added R504: 1k, Resistor_SMD:R_0805_2012Metric_Pad1.20x1.40mm_HandSolder, F.Cu at (711.0, 104.5)
- added R505: 10k, Resistor_SMD:R_0805_2012Metric_Pad1.20x1.40mm_HandSolder, F.Cu at (711.0, 107.5)
- added R601: 10k, Resistor_SMD:R_0805_2012Metric_Pad1.20x1.40mm_HandSolder, F.Cu at (677.1, 90.0)
- added R602: 10k, Resistor_SMD:R_0805_2012Metric_Pad1.20x1.40mm_HandSolder, F.Cu at (677.1, 92.9)
- added REF**: MountingHole_3.2mm_M3, MountingHole:MountingHole_3.2mm_M3, F.Cu at (42.5, 37.5)
- added REF**: MountingHole_3.2mm_M3, MountingHole:MountingHole_3.2mm_M3, F.Cu at (262.5, 257.5)
- added REF**: MountingHole_3.2mm_M3, MountingHole:MountingHole_3.2mm_M3, F.Cu at (42.5, 257.5)
- added REF**: MountingHole_3.2mm_M3, MountingHole:MountingHole_3.2mm_M3, F.Cu at (262.5, 37.5)
- added SW301: SW_Push, Button_Switch_SMD:SW_SPST_PTS810, F.Cu at (527.1, 63.5)
- added SW302: SW_Push, Button_Switch_SMD:SW_SPST_PTS810, F.Cu at (527.1, 68.3)
- added U201: CP2102N-Axx-xQFN24, Package_DFN_QFN:QFN-24-1EP_4x4mm_P0.5mm_EP2.6x2.6mm_ThermalVias, F.Cu at (733.1, 148.8)
- added U301: ESP32-C3-WROOM-02, RF_Module:ESP32-C3-WROOM-02, F.Cu at (533.8, 53.5)
- added U302: TLV1117LV33, Package_TO_SOT_SMD:SOT-223-3_TabPin2, F.Cu at (535.4, 65.4)
- added U401: DS3231M, Package_SO:SOIC-16W_7.5x10.3mm_P1.27mm, F.Cu at (659.8, 212.7)
- added U501: BH1750xxx-xx, Package_TO_SOT_SMD:HVSOF6, F.Cu at (715.6, 104.7)
- moved G0 255.9 mm to (253.5, 253.0)
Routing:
- net +5V: track 0.00 -> 274.1 mm
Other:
- board size 100 x 100 mm -> 235 x 235 mm

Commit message: Add: Componentes and created first routes
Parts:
- BT401, C201, C202, C203, C204, C205, C206, C207, C208, C301, C302, C305, C306, C307, C308, C309, C401, C402, C403, C404, C501, C502, C503, C504, C505, D201, D202, D203, J101, J201, JP501, Q201, Q202, R201, R204, R205, R206, R207, R208, R209, R210, R211, R212, R213, R214, R401, R402, R403, R404, R405, R501, R502, R503, R504, R505, U201, U301, U302, U401, U501: moved to B.Cu
- moved D202 659.0 mm to (88.5, 35.9), turned to 180 degrees
- moved D203 659.0 mm to (88.5, 39.0), turned to 180 degrees
- moved R213 653.2 mm to (84.1, 35.8)
- moved R214 653.2 mm to (84.1, 39.2)
- moved Q601 625.4 mm to (53.0, 61.8)
- moved R601 625.4 mm to (52.2, 65.5)
- moved R602 625.4 mm to (52.2, 68.5)
- moved U201 615.8 mm to (127.5, 37.2)
- moved R209 614.7 mm to (118.6, 38.2), turned to 180 degrees
- moved R208 614.5 mm to (118.6, 36.2), turned to 180 degrees
- moved Q202 613.7 mm to (126.5, 55.0), turned to 180 degrees
- moved Q201 613.3 mm to (127.0, 49.5), turned to 180 degrees
- moved R206 609.4 mm to (125.6, 21.4), turned to 180 degrees
- moved R207 609.4 mm to (125.6, 24.4), turned to 180 degrees
- moved R210 605.0 mm to (131.3, 27.0), turned to 180 degrees
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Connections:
- net Net-(D201-K-Pad2) renamed /USB/USB_{IN}.D+
- net Net-(D201-K-Pad3) renamed /USB/USB_{IN}.D-
- net Net-(U201-D+) renamed /USB/USB_{0}.D+
- net Net-(U201-D-) renamed /USB/USB_{0}.D-
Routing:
- net +3V3: track 0.00 -> 35.5 mm, vias 0 -> 2
- net GND: track 0.00 -> 23.5 mm, vias 0 -> 6
- net /USB/USB_{IN}.D-: track 0.00 -> 6.51 mm
- net +5V: track 274.1 -> 280.6 mm, vias 0 -> 10
- net Net-(U201-VBUS): track 0.00 -> 5.70 mm
- net /USB/USB_{IN}.D+: track 0.00 -> 5.63 mm
- net /USB/USB_{0}.D+: track 0.00 -> 5.17 mm
- net /USB/USB_{0}.D-: track 0.00 -> 5.17 mm
- net /Brightness Sensor/~{RST}: track 0.00 -> 4.54 mm
- net +BATT: track 0.00 -> 4.53 mm
- net Net-(J201-CC1): track 0.00 -> 3.90 mm, vias 0 -> 1
- net Net-(J201-CC2): track 0.00 -> 3.69 mm, vias 0 -> 1
- net /MCU/USB.D-: track 0.00 -> 2.13 mm
- net /MCU/USB.D+: track 0.00 -> 2.13 mm
- net Net-(U201-~{RST}): track 0.00 -> 1.93 mm
- added copper zone on B.Cu, net +5V
- added copper zone on B.Cu, net Net-(J201-SHIELD)

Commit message: Mod: Almost finished layout for the USB-C
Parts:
- Q601, R601, R602: moved to B.Cu
- moved R206 232.6 mm to (136.7, 253.7), turned to 90 degrees
- moved R207 229.7 mm to (138.7, 253.7), turned to -90 degrees
- moved Q201 229.3 mm to (103.0, 277.6)
- moved R212 227.6 mm to (105.8, 280.4), turned to 180 degrees
- moved R211 227.5 mm to (105.8, 274.8)
- moved R213 224.9 mm to (130.0, 256.0), turned to 90 degrees
- moved R210 223.6 mm to (137.6, 250.5), turned to 0 degrees
- moved C202 223.4 mm to (143.7, 254.1), turned to 180 degrees
- moved Q202 223.3 mm to (108.6, 277.6), turned to 0 degrees
- moved R214 222.2 mm to (133.0, 256.0), turned to 90 degrees
- moved C204 222.2 mm to (147.6, 252.9), turned to 0 degrees
- moved C203 221.5 mm to (140.7, 253.7), turned to -90 degrees
- moved D202 220.0 mm to (130.0, 252.0), turned to -90 degrees
- moved C206 219.3 mm to (143.7, 252.0), turned to 180 degrees
- moved C207 218.0 mm to (147.6, 250.8), turned to 0 degrees
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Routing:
- net /MCU/USB.D+: track 2.13 -> 409.9 mm
- net /MCU/USB.D-: track 2.13 -> 406.3 mm
- net /MCU/UART.RXD: track 0.00 -> 101.6 mm
- net /MCU/UART.TXD: track 0.00 -> 100.2 mm
- net /LEDs/LED11-1/D_{IN}: track 0.00 -> 98.4 mm, vias 0 -> 1
- net +3V3: track 35.5 -> 55.1 mm, vias 2 -> 8
- net Net-(Q201-E): track 0.00 -> 19.0 mm, vias 0 -> 2
- net /USB/USB_{IN}.D-: track 6.51 -> 19.8 mm
- net Net-(D202-K): track 0.00 -> 12.6 mm
- net GND: track 23.5 -> 34.5 mm
- net /USB/USB_{IN}.D+: track 5.63 -> 16.3 mm
- net Net-(Q202-E): track 0.00 -> 10.6 mm
- net Net-(D203-K): track 0.00 -> 9.44 mm
- net /LEDs/LED_{IN}: track 0.00 -> 6.13 mm
- net +5V: track 280.6 -> 284.8 mm, vias 10 -> 12
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
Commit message: Mod: Layout, finished the layout. Changed the voltage pins of J101
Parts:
- added G***: LOGO, Drawing_User:elektronik-emblem_20x23.1_solder, B.Cu at (67.0, 46.0)
- C303, C304, D301, D302, R301, R302, R303, R304, SW301, SW302: moved to B.Cu
- moved Q202 253.0 mm to (173.5, 33.0), turned to 90 degrees
- moved R212 252.3 mm to (174.6, 37.6), turned to -90 degrees
- moved R211 246.3 mm to (172.4, 37.6), turned to 90 degrees
- moved Q201 245.7 mm to (173.5, 42.2), turned to -90 degrees
- moved D301 241.7 mm to (92.0, 38.0), turned to -90 degrees
- moved R304 237.8 mm to (96.0, 38.0), turned to -90 degrees
- moved D302 237.6 mm to (96.0, 42.0), turned to 90 degrees
- moved R303 236.4 mm to (92.0, 42.0), turned to 90 degrees
- moved R302 127.1 mm to (164.2, 39.9), turned to 180 degrees
- moved R301 115.5 mm to (166.4, 35.1), turned to 180 degrees
- moved G0 111.1 mm to (174.8, 278.5)
- moved C303 108.7 mm to (178.1, 33.0), turned to -90 degrees
- moved C304 100.1 mm to (178.1, 42.2), turned to 90 degrees
- moved SW301 98.2 mm to (182.0, 33.0)
- moved SW302 97.3 mm to (182.0, 42.2), turned to 180 degrees
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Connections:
- J101 pad 7: +3V3 -> +5V
- J101 pad 8: +5V -> +3V3
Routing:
- net /Brightness Sensor/LDR: track 0.00 -> 390.5 mm, vias 0 -> 1
- net /Brightness Sensor/I^{2}C.SDA: track 0.00 -> 355.4 mm, vias 0 -> 2
- net /Brightness Sensor/I^{2}C.SCL: track 0.00 -> 354.0 mm
- net /Brightness Sensor/~{RST}: track 4.54 -> 347.0 mm, vias 0 -> 4
- net GND: track 34.5 -> 346.3 mm, vias 6 -> 359
- net Net-(Q202-E): track 10.6 -> 240.7 mm, vias 0 -> 4
- net Net-(Q201-E): track 19.0 -> 240.5 mm, vias 2 -> 4
- net /MCU/USB.D-: track 406.3 -> 210.1 mm
- net /MCU/USB.D+: track 409.9 -> 214.0 mm
- net /MCU/IO1: track 0.00 -> 111.5 mm, vias 0 -> 4
- net /MCU/UART.TXD: track 100.2 -> 208.4 mm, vias 0 -> 2
- net /MCU/IO4: track 0.00 -> 107.2 mm, vias 0 -> 4
- net /MCU/UART.RXD: track 101.6 -> 206.9 mm, vias 0 -> 2
- net /LEDs/LED04-1/D_{IN}: track 0.00 -> 54.5 mm
- net /MCU/IO0: track 0.00 -> 43.3 mm
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- added copper zone on F.Cu, net +3V3
- added copper zone on F.Cu, net +5V
- added copper zone on B.Cu, net GND
- added copper zone on F.Cu, net GND
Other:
- board text added: "3.3V"
- board text added: "5V"
- board text added: "BOOT"
- board text added: "RST"
- board text added: "RX"
- board text added: "TX"

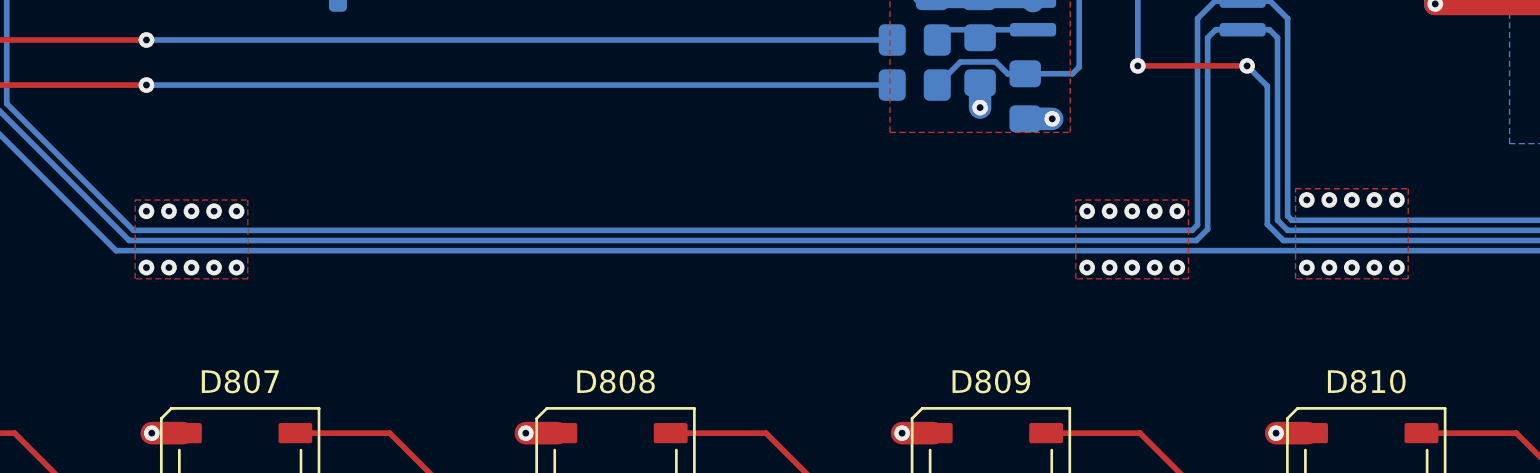
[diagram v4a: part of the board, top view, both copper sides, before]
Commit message: Fix: ESP-Wordclock.kicad_pcb, run DRC and fixed errors
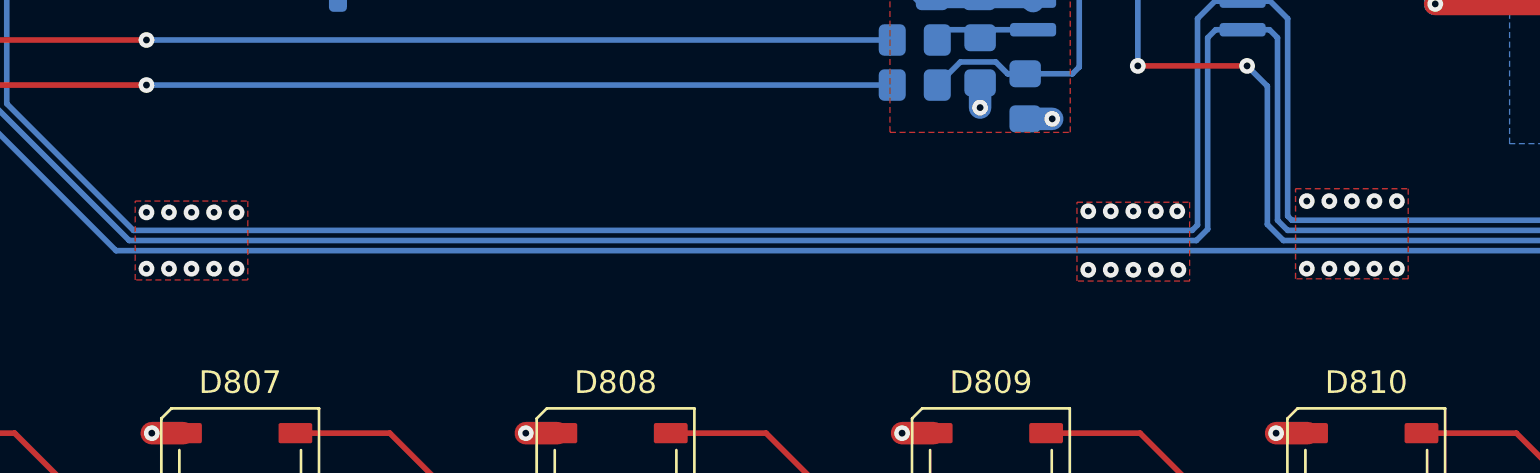
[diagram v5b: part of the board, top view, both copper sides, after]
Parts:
- removed G0: LOGO, drawings:elektronik-emblem_3x3.5_solder
